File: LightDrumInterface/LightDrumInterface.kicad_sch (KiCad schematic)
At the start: 59 parts, among them J1 Conn_01x04_Male, J2 DEBUG-CONN, J3 Conn_01x04_Male, J4 B24B-PHDSS(LF)(SN), J5 B24B-PHDSS(LF)(SN), SW1 RESET-SW, U1 STP16CP05, U2 TPL0401B-10-Q1, U3 74AUP2G04, U4 PC817

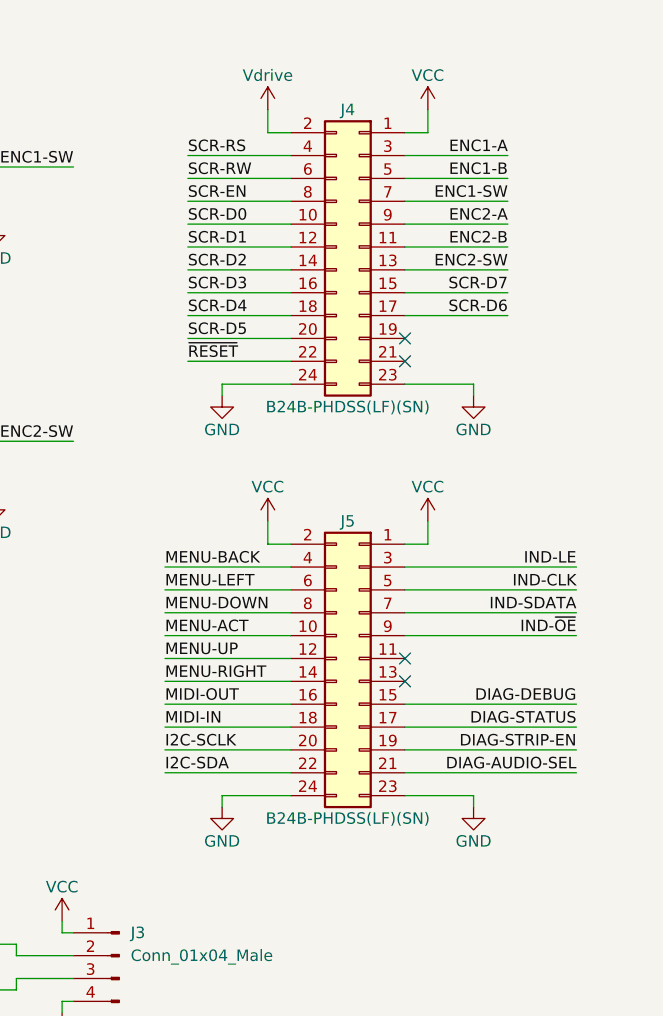
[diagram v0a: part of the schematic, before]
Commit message: Replace interface harnesses with FPC cable
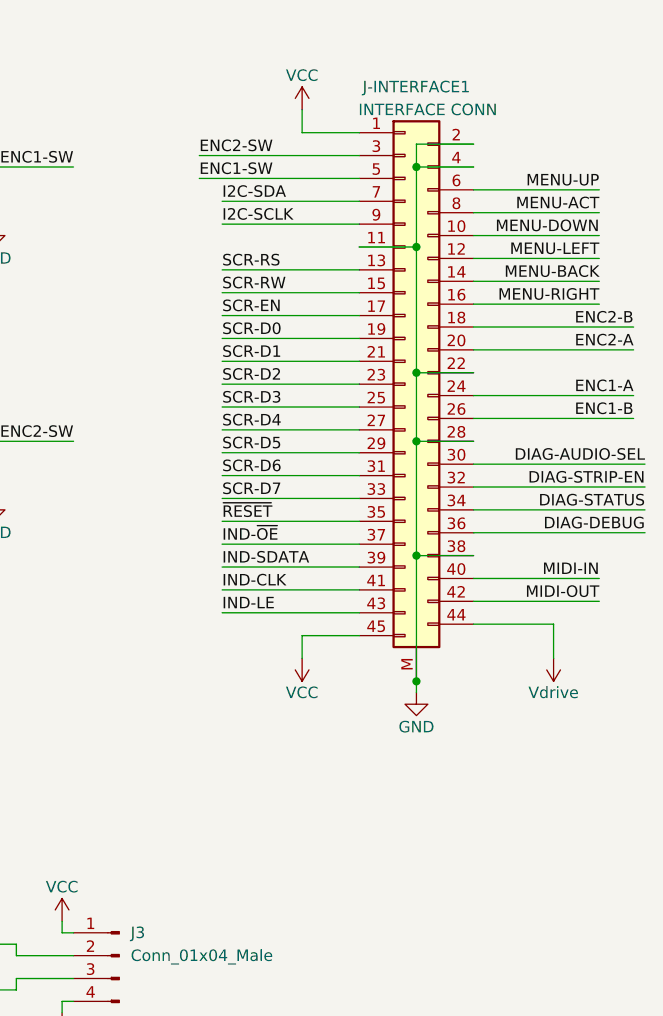
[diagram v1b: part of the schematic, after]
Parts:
- removed J4, J5: B24B-PHDSS(LF)(SN), Daxxn_Connectors:B24B-PHDSS(LF)(SN), symbol Connector_Generic:Conn_02x12_Odd_Even
- added J-INTERFACE1: INTERFACE CONN, Daxxn_Connectors:5025984593, symbol Daxxn_Connectors:Conn_2-45-M_Odd_Even
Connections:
- net DIAG-AUDIO-SEL: now also J-INTERFACE1.30 (Pin_30)
- net DIAG-DEBUG: now also J-INTERFACE1.36 (Pin_36)
- net DIAG-STATUS: now also J-INTERFACE1.34 (Pin_34)
- net DIAG-STRIP-EN: now also J-INTERFACE1.32 (Pin_32)
- net ENC1-A: now also J-INTERFACE1.24 (Pin_24)
- net ENC1-B: now also J-INTERFACE1.26 (Pin_26)
- net ENC1-SW: now also J-INTERFACE1.5 (Pin_5)
- net ENC2-A: now also J-INTERFACE1.20 (Pin_20)
- net ENC2-B: now also J-INTERFACE1.18 (Pin_18)
- net ENC2-SW: now also J-INTERFACE1.3 (Pin_3)
- net GND: now also J-INTERFACE1.11 (Pin_11), J-INTERFACE1.2 (Pin_2), J-INTERFACE1.22 (Pin_22), J-INTERFACE1.28 (Pin_28), J-INTERFACE1.38 (Pin_38), J-INTERFACE1.4 (Pin_4), J-INTERFACE1.M (MNT)
- net I2C-SCLK: now also J-INTERFACE1.9 (Pin_9)
- net I2C-SDA: now also J-INTERFACE1.7 (Pin_7)
- net IND-CLK: now also J-INTERFACE1.41 (Pin_41)
- net IND-LE: now also J-INTERFACE1.43 (Pin_43)
- net IND-SDATA: now also J-INTERFACE1.39 (Pin_39)
- net IND-~{OE}: now also J-INTERFACE1.37 (Pin_37)
- net MENU-ACT: now also J-INTERFACE1.8 (Pin_8)
- net MENU-BACK: now also J-INTERFACE1.14 (Pin_14)
- net MENU-DOWN: now also J-INTERFACE1.10 (Pin_10)
- net MENU-LEFT: now also J-INTERFACE1.12 (Pin_12)
- net MENU-RIGHT: now also J-INTERFACE1.16 (Pin_16)
- net MENU-UP: now also J-INTERFACE1.6 (Pin_6)
- net MIDI-IN: now also J-INTERFACE1.40 (Pin_40)
- net MIDI-OUT: now also J-INTERFACE1.42 (Pin_42)
- net SCR-D0: now also J-INTERFACE1.19 (Pin_19)
- net SCR-D1: now also J-INTERFACE1.21 (Pin_21)
- net SCR-D2: now also J-INTERFACE1.23 (Pin_23)
- net SCR-D3: now also J-INTERFACE1.25 (Pin_25)
- net SCR-D4: now also J-INTERFACE1.27 (Pin_27)
- net SCR-D5: now also J-INTERFACE1.29 (Pin_29)
- net SCR-D6: now also J-INTERFACE1.31 (Pin_31)
- net SCR-D7: now also J-INTERFACE1.33 (Pin_33)
- net SCR-EN: now also J-INTERFACE1.17 (Pin_17)
- net SCR-RS: now also J-INTERFACE1.13 (Pin_13)
- net SCR-RW: now also J-INTERFACE1.15 (Pin_15)
- net VCC: now also J-INTERFACE1.1 (Pin_1), J-INTERFACE1.45 (Pin_45)
- net Vdrive: now also J-INTERFACE1.44 (Pin_44)
- net ~{RESET}: now also J-INTERFACE1.35 (Pin_35)
- no-connect marks 7 -> 3

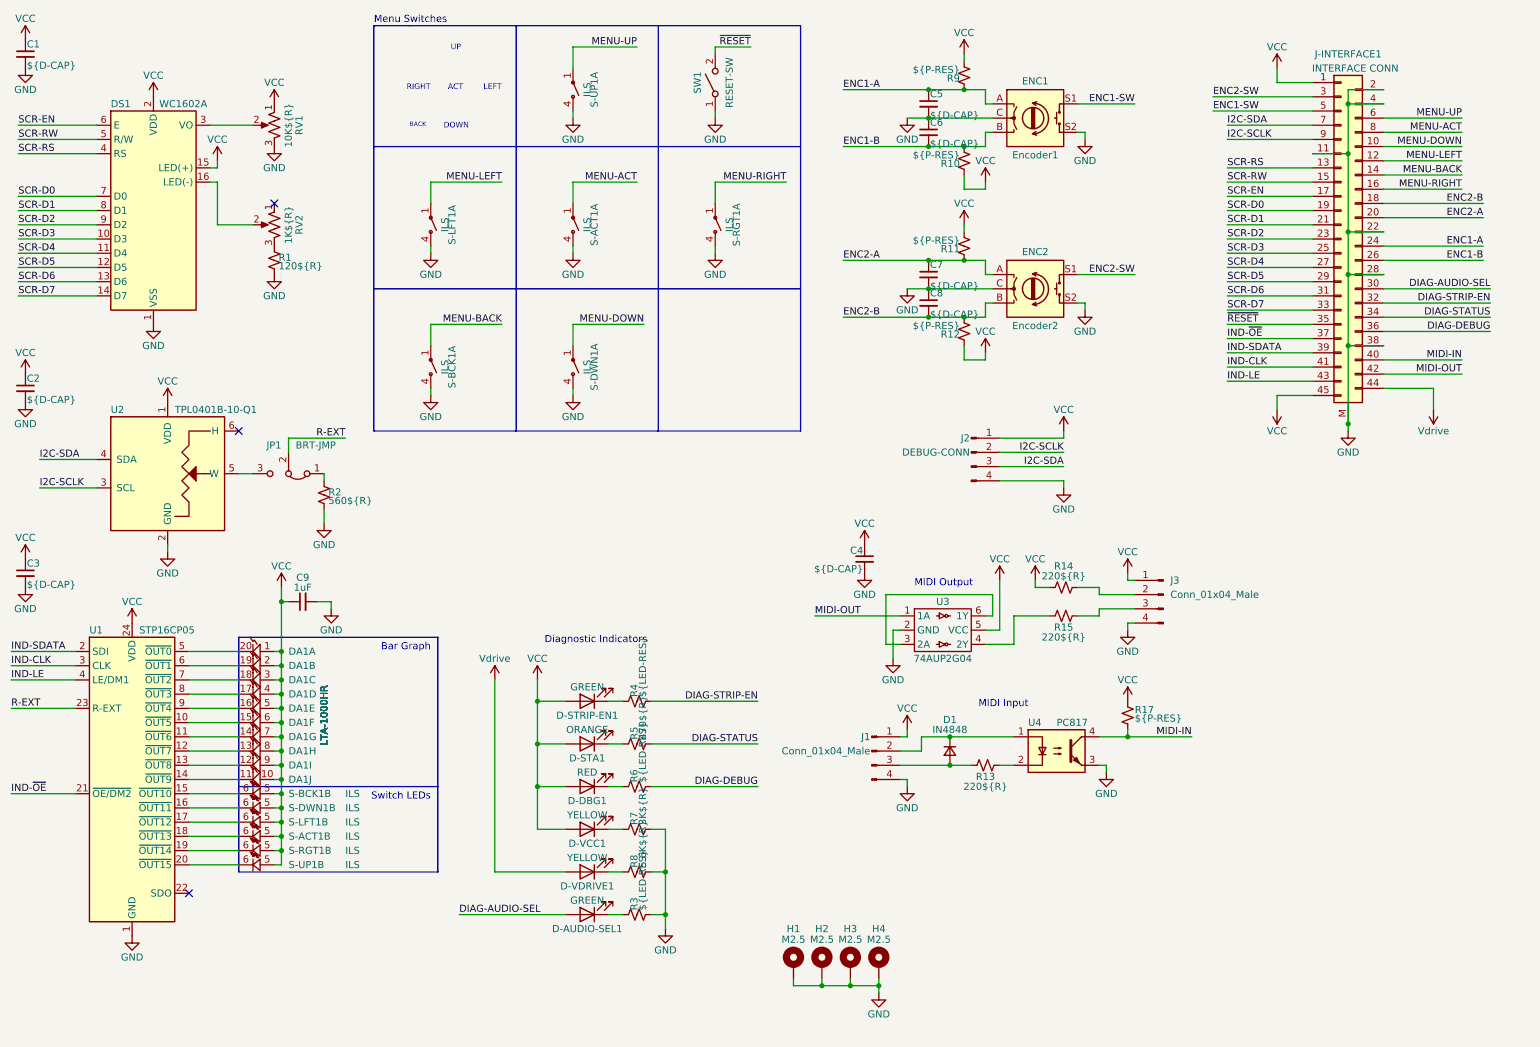
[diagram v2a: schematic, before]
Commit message: Replace screen (WIP)
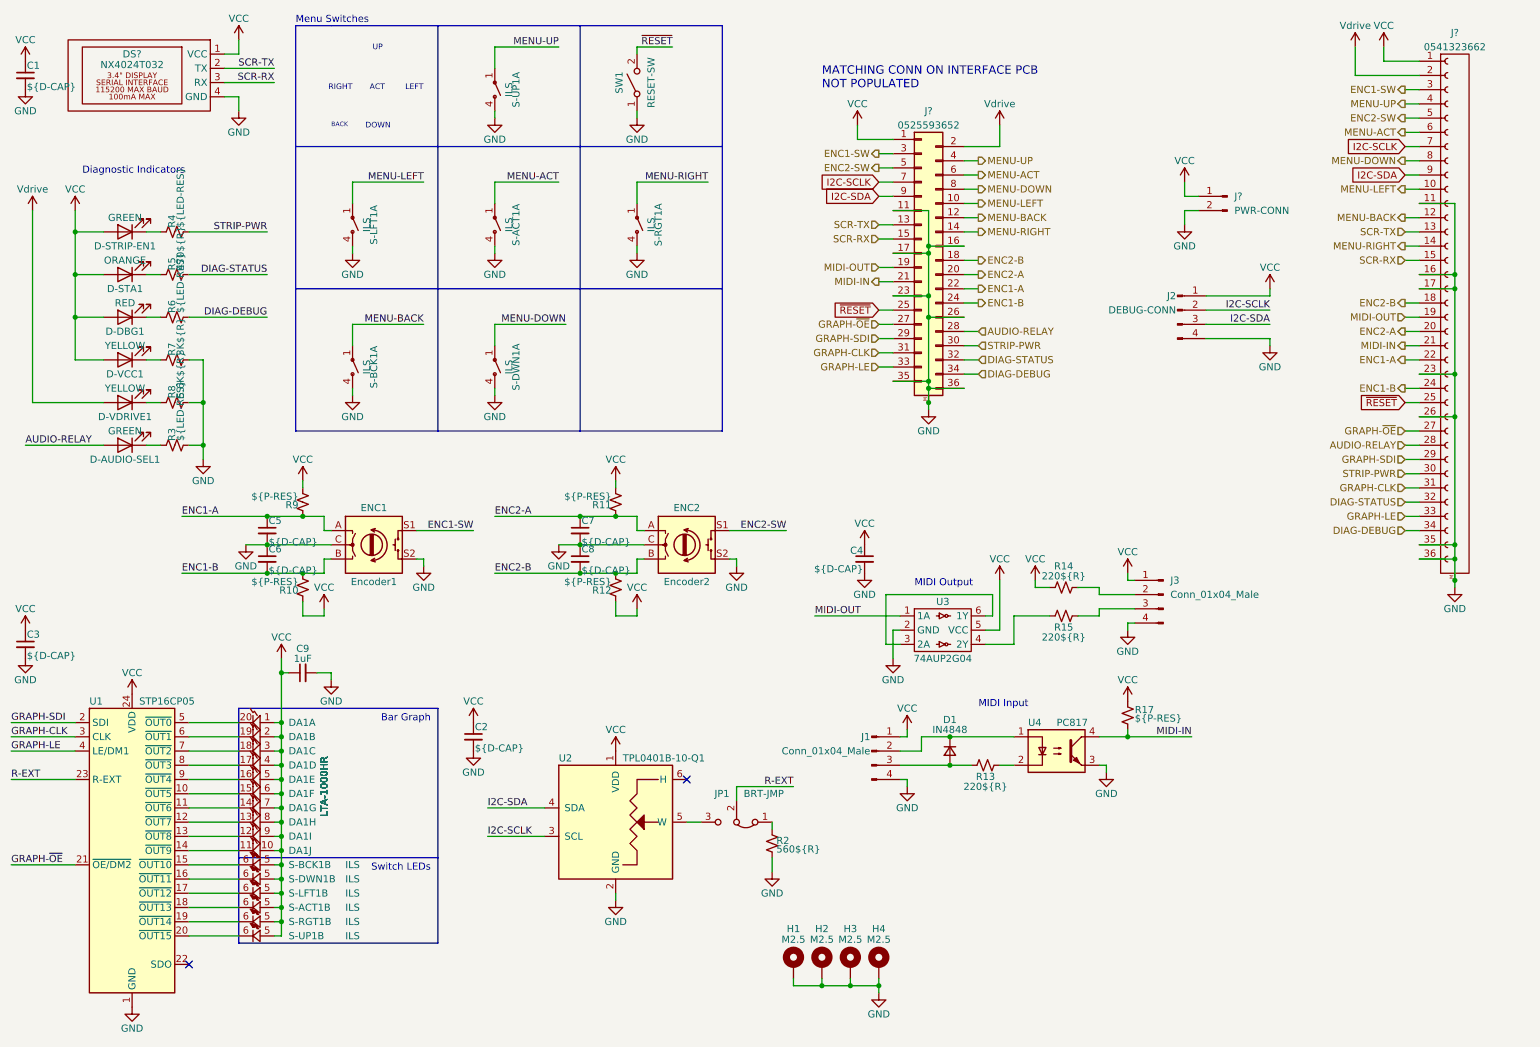
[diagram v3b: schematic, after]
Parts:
- removed DS1: WC1602A, Display:WC1602A, symbol Display_Character:WC1602A
- removed J-INTERFACE1: INTERFACE CONN, Daxxn_Connectors:5025984593, symbol Daxxn_Connectors:Conn_2-45-M_Odd_Even
- removed R1: 120${R}, Resistor_SMD:R_0805_2012Metric, symbol Device:R_Small_US
- removed RV1: 10K${R}, Daxxn_Switches:PT01-D120K2-B103, symbol Device:R_Potentiometer_US
- removed RV2: 1K${R}, Daxxn_Switches:PT01-D120K2-B103, symbol Device:R_Potentiometer_US
- added DS?: NX4024T032, Daxxn_Displays:NX4024T032_10mm, symbol Daxxn_Displays:NX4024T032
- added J?: 0541323662, Daxxn_Connectors:0541323662, symbol Daxxn_Connectors:0541323662
- added J?: 0525593652, Daxxn_Connectors:0525593652, symbol Daxxn_Connectors:0525593652
- added J?: PWR-CONN, Connector_JST:JST_XA_B02B-XASK-1_1x02_P2.50mm_Vertical, symbol Connector:Conn_01x02_Male
- D-AUDIO-SEL1, D-DBG1, D-STA1, D-STRIP-EN1, D-VCC1, D-VDRIVE1: footprint Daxxn_LEDs:LED_PLCC-2 -> LED_SMD:LED_0805_2012Metric
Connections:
- net DIAG-DEBUG: now also J?.34 (Pin_34), J?.34 (Pin_34)
- net DIAG-STATUS: now also J?.32 (Pin_32), J?.32 (Pin_32)
- net ENC1-A: now also J?.22 (Pin_22), J?.22 (Pin_22)
- net ENC1-B: now also J?.24 (Pin_24), J?.24 (Pin_24)
- net ENC1-SW: now also J?.3 (Pin_3), J?.3 (Pin_3)
- net ENC2-A: now also J?.20 (Pin_20), J?.20 (Pin_20)
- net ENC2-B: now also J?.18 (Pin_18), J?.18 (Pin_18)
- net ENC2-SW: now also J?.5 (Pin_5), J?.5 (Pin_5)
- net GND: now also DS?.4 (GND), J?.11 (Pin_11), J?.11 (Pin_11), J?.16 (Pin_16), J?.16 (Pin_16), J?.17 (Pin_17), J?.17 (Pin_17), J?.2 (Pin_2), J?.23 (Pin_23), J?.23 (Pin_23), J?.26 (Pin_26), J?.26 (Pin_26), J?.35 (Pin_35), J?.35 (Pin_35), J?.36 (Pin_36), J?.36 (Pin_36), J?.M (MNT), J?.M (MNT)
- net I2C-SCLK: now also J?.7 (Pin_7), J?.7 (Pin_7)
- net I2C-SDA: now also J?.9 (Pin_9), J?.9 (Pin_9)
- net MENU-ACT: now also J?.6 (Pin_6), J?.6 (Pin_6)
- net MENU-BACK: now also J?.12 (Pin_12), J?.12 (Pin_12)
- net MENU-DOWN: now also J?.8 (Pin_8), J?.8 (Pin_8)
- net MENU-LEFT: now also J?.10 (Pin_10), J?.10 (Pin_10)
- net MENU-RIGHT: now also J?.14 (Pin_14), J?.14 (Pin_14)
- net MENU-UP: now also J?.4 (Pin_4), J?.4 (Pin_4)
- net MIDI-IN: now also J?.21 (Pin_21), J?.21 (Pin_21)
- net MIDI-OUT: now also J?.19 (Pin_19), J?.19 (Pin_19)
- net VCC: now also DS?.1 (VCC), J?.1 (Pin_1), J?.1 (Pin_1), J?.1 (Pin_1)
- net Vdrive: now also J?.2 (Pin_2), J?.2 (Pin_2)
- net ~{RESET}: now also J?.25 (Pin_25), J?.25 (Pin_25)
- net DIAG-AUDIO-SEL renamed AUDIO-RELAY
- net AUDIO-RELAY: now also J?.28 (Pin_28), J?.28 (Pin_28)
- net DIAG-STRIP-EN renamed STRIP-PWR
- net STRIP-PWR: now also J?.30 (Pin_30), J?.30 (Pin_30)
- net IND-CLK renamed GRAPH-CLK
- net GRAPH-CLK: now also J?.31 (Pin_31), J?.31 (Pin_31)
- net IND-LE renamed GRAPH-LE
- net GRAPH-LE: now also J?.33 (Pin_33), J?.33 (Pin_33)
- net IND-SDATA renamed GRAPH-SDI
- net GRAPH-SDI: now also J?.29 (Pin_29), J?.29 (Pin_29)
- net IND-~{OE} renamed GRAPH-~{OE}
- net GRAPH-~{OE}: now also J?.27 (Pin_27), J?.27 (Pin_27)
- new net SCR-RX: DS?.3 (RX), J?.15 (Pin_15), J?.15 (Pin_15)
- new net SCR-TX: DS?.2 (TX), J?.13 (Pin_13), J?.13 (Pin_13)
- no-connect marks 3 -> 2
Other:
- note added: "MATCHING CONN ON INTERFACE PCB NOT POPULATED"
- moved on the sheet: C1, C2, C3, C5, C6, C7, C8, C9, D-AUDIO-SEL1, D-DBG1, D-STA1, D-STRIP-EN1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

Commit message: Replaced display and FPC cable
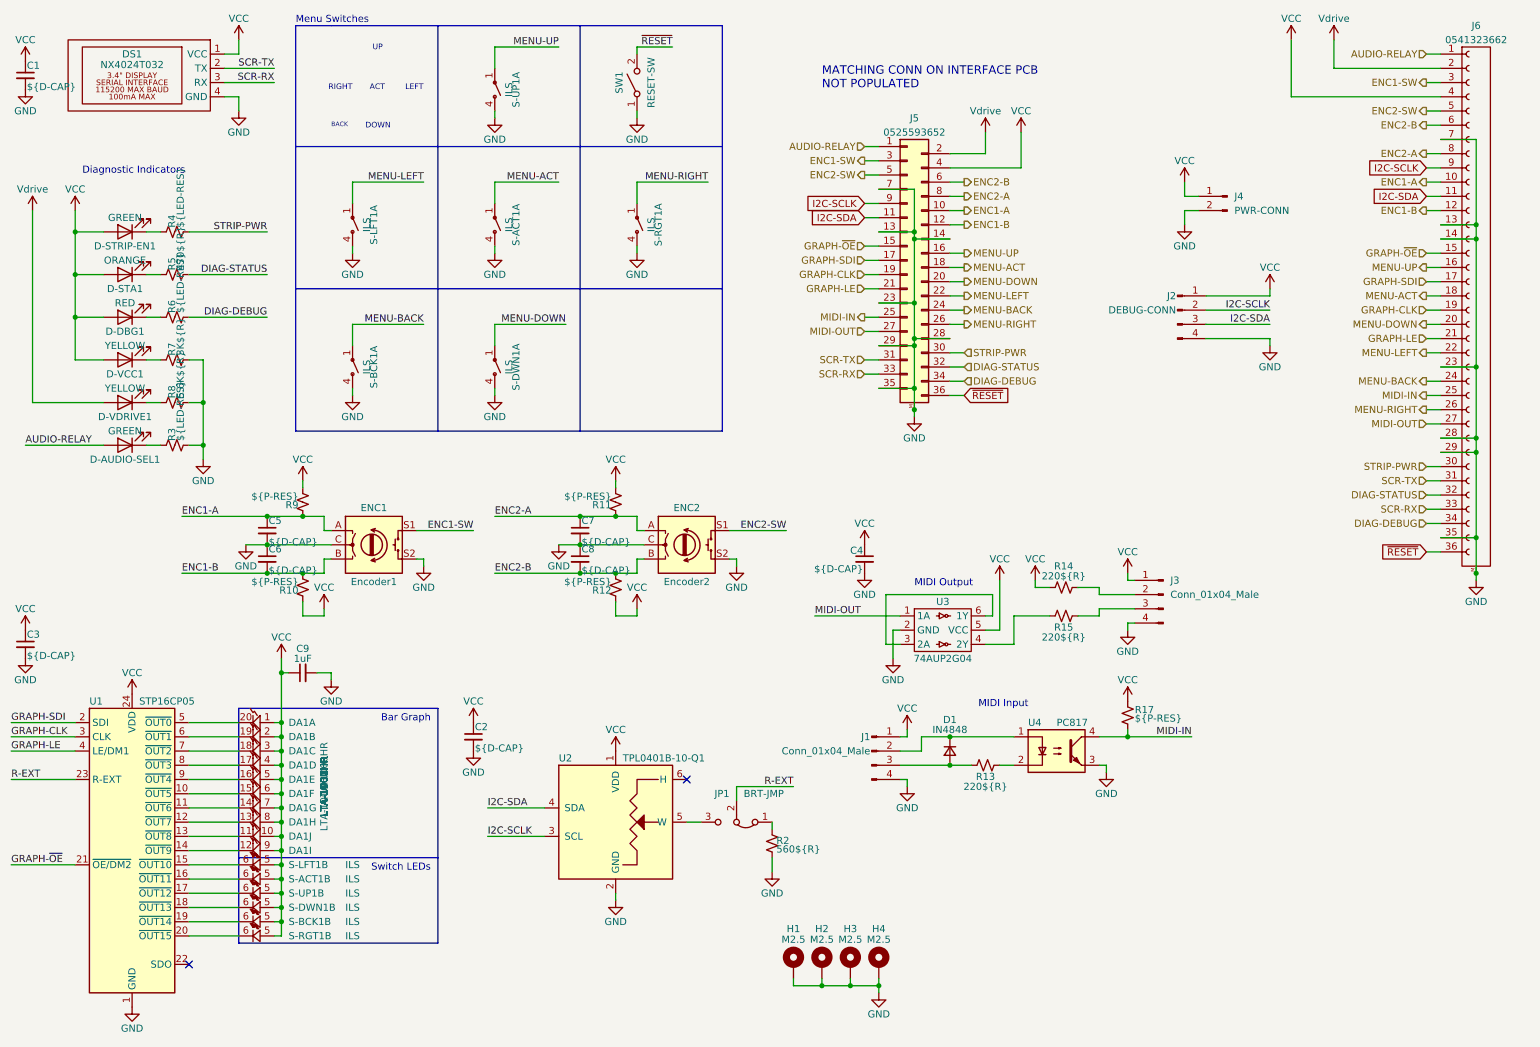
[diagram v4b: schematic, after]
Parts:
- removed J?: 0541323662, Daxxn_Connectors:0541323662, symbol Daxxn_Connectors:0541323662
- removed J?: 0525593652, Daxxn_Connectors:0525593652, symbol Daxxn_Connectors:0525593652
- added J5: 0525593652, Daxxn_Connectors:0525593652, symbol Daxxn_Connectors:0525593652
- added J6: 0541323662, Daxxn_Connectors:0541323662, symbol Daxxn_Connectors:0541323662
- DS1: renamed from DS?; footprint Daxxn_Displays:NX4024T032_10mm -> Daxxn_Displays:NX4024T032_10mm_Harness
- gave numbers to parts that had none: 1
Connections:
- net AUDIO-RELAY: now also J5.1 (Pin_1), J6.1 (Pin_1)
- net DIAG-DEBUG: now also J5.34 (Pin_34), J6.34 (Pin_34)
- net DIAG-STATUS: now also J5.32 (Pin_32), J6.32 (Pin_32)
- net ENC1-A: now also J5.10 (Pin_10), J6.10 (Pin_10)
- net ENC1-B: now also J5.12 (Pin_12), J6.12 (Pin_12)
- net ENC1-SW: now also J5.3 (Pin_3), J6.3 (Pin_3)
- net ENC2-A: now also J5.8 (Pin_8), J6.8 (Pin_8)
- net ENC2-B: now also J5.6 (Pin_6), J6.6 (Pin_6)
- net ENC2-SW: now also J5.5 (Pin_5), J6.5 (Pin_5)
- net GND: now also J5.13 (Pin_13), J5.14 (Pin_14), J5.23 (Pin_23), J5.28 (Pin_28), J5.29 (Pin_29), J5.35 (Pin_35), J5.7 (Pin_7), J5.M (MNT), J6.13 (Pin_13), J6.14 (Pin_14), J6.23 (Pin_23), J6.28 (Pin_28), J6.29 (Pin_29), J6.35 (Pin_35), J6.7 (Pin_7), J6.M (MNT)
- net GRAPH-CLK: now also J5.19 (Pin_19), J6.19 (Pin_19)
- net GRAPH-LE: now also J5.21 (Pin_21), J6.21 (Pin_21)
- net GRAPH-SDI: now also J5.17 (Pin_17), J6.17 (Pin_17)
- net GRAPH-~{OE}: now also J5.15 (Pin_15), J6.15 (Pin_15)
- net I2C-SCLK: now also J5.9 (Pin_9), J6.9 (Pin_9)
- net I2C-SDA: now also J5.11 (Pin_11), J6.11 (Pin_11)
- net MENU-ACT: now also J5.18 (Pin_18), J6.18 (Pin_18)
- net MENU-BACK: now also J5.24 (Pin_24), J6.24 (Pin_24)
- net MENU-DOWN: now also J5.20 (Pin_20), J6.20 (Pin_20)
- net MENU-LEFT: now also J5.22 (Pin_22), J6.22 (Pin_22)
- net MENU-RIGHT: now also J5.26 (Pin_26), J6.26 (Pin_26)
- net MENU-UP: now also J5.16 (Pin_16), J6.16 (Pin_16)
- net MIDI-IN: now also J5.25 (Pin_25), J6.25 (Pin_25)
- net MIDI-OUT: now also J5.27 (Pin_27), J6.27 (Pin_27)
- net SCR-RX: now also J5.33 (Pin_33), J6.33 (Pin_33)
- net SCR-TX: now also J5.31 (Pin_31), J6.31 (Pin_31)
- net STRIP-PWR: now also J5.30 (Pin_30), J6.30 (Pin_30)
- net VCC: now also J5.4 (Pin_4), J6.4 (Pin_4)
- net Vdrive: now also J5.2 (Pin_2), J6.2 (Pin_2)
- net ~{RESET}: now also J5.36 (Pin_36), J6.36 (Pin_36)
- net at S-BCK1.6: now also U1.19 (~{OUT14}); no longer U1.15 (~{OUT10})
- net at S-DWN1.6: now also U1.18 (~{OUT13}); no longer U1.16 (~{OUT11})
- net at DA1.11: now also U1.13 (~{OUT8}); no longer U1.14 (~{OUT9})
- net at S-RGT1.6: now also U1.20 (~{OUT15}); no longer U1.19 (~{OUT14})
- net at DA1.12: now also U1.14 (~{OUT9}); no longer U1.13 (~{OUT8})
- net at S-LFT1.6: now also U1.15 (~{OUT10}); no longer U1.17 (~{OUT12})
- net at S-ACT1.6: now also U1.16 (~{OUT11}); no longer U1.18 (~{OUT13})
- net at S-UP1.6: now also U1.17 (~{OUT12}); no longer U1.20 (~{OUT15})
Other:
- moved on the sheet: DA1I, DA1J, S-ACT1B, S-BCK1B, S-DWN1B, S-LFT1B, S-RGT1B, S-UP1B
